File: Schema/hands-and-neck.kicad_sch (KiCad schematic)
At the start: 17 parts, among them U1 Left Arm Rotation X, U10 Right Arm Rotation Y, U11 Right Arm Rotation X, U12 Right Arm Rotation Z, U13 Right Elbow, U14 Neck Y, U15 Left Arm Rotation Y, U16 Neck Z, U2 Left Arm Rotation Z, U5 Left Elbow, U6 Left Wrist, U7 Left Claw, U8 Right Wrist, U9 Right Claw

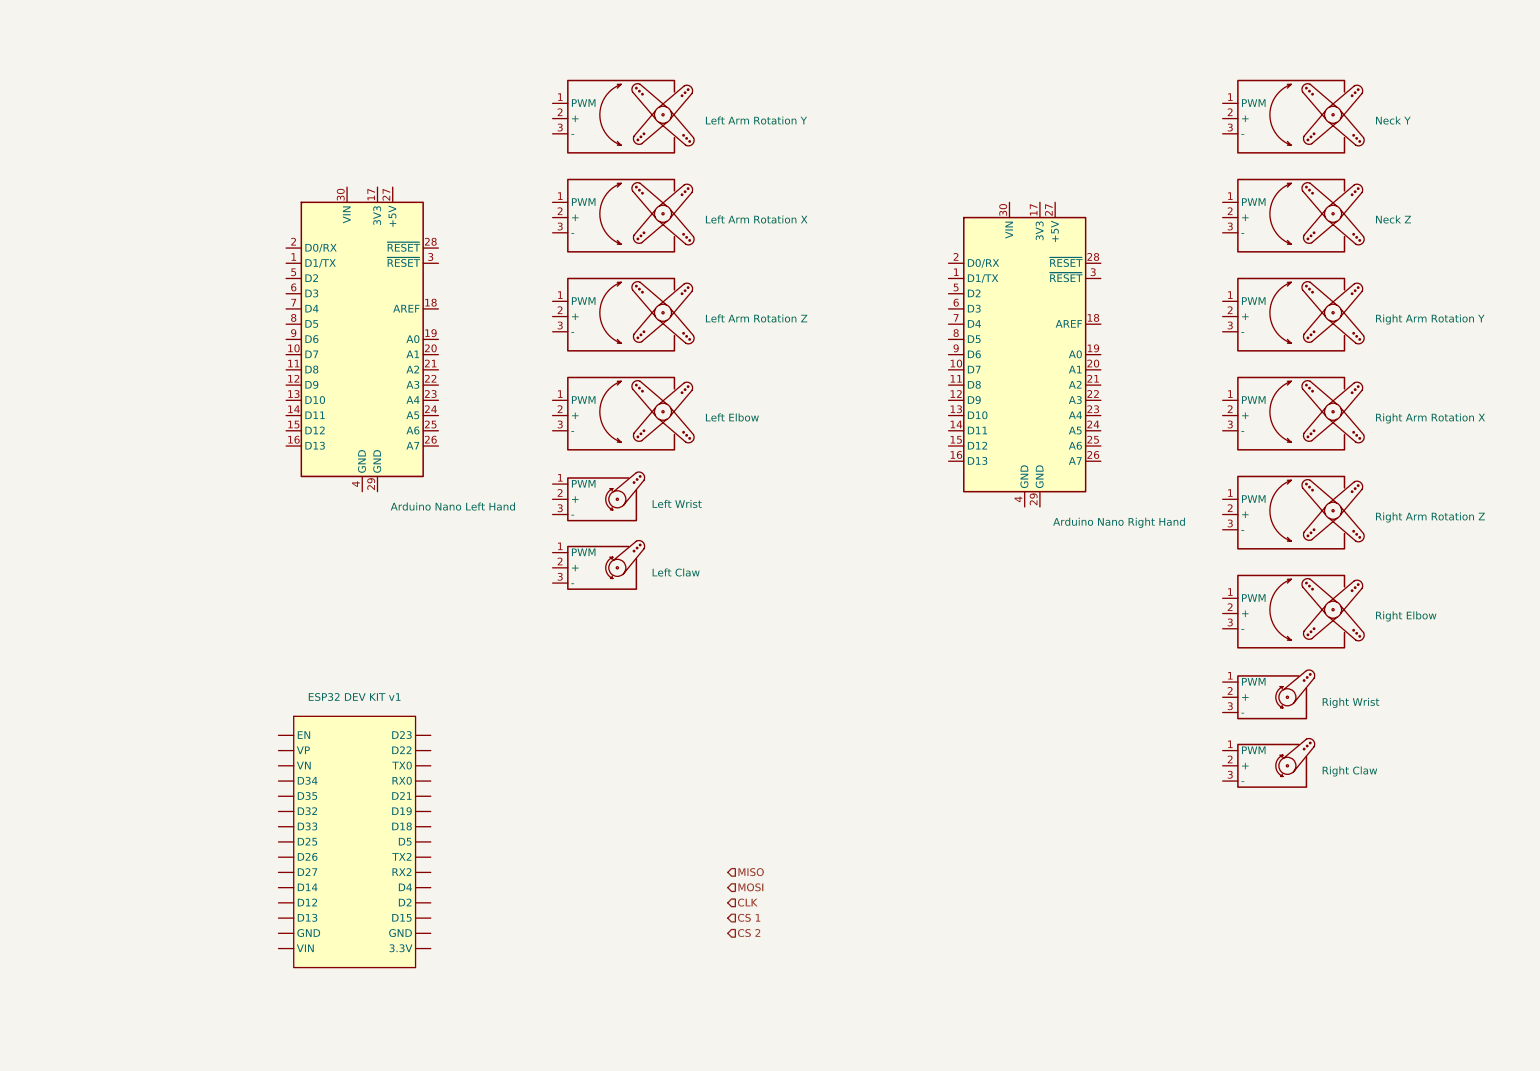
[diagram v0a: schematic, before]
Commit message: Updated schema and added math before ONCS
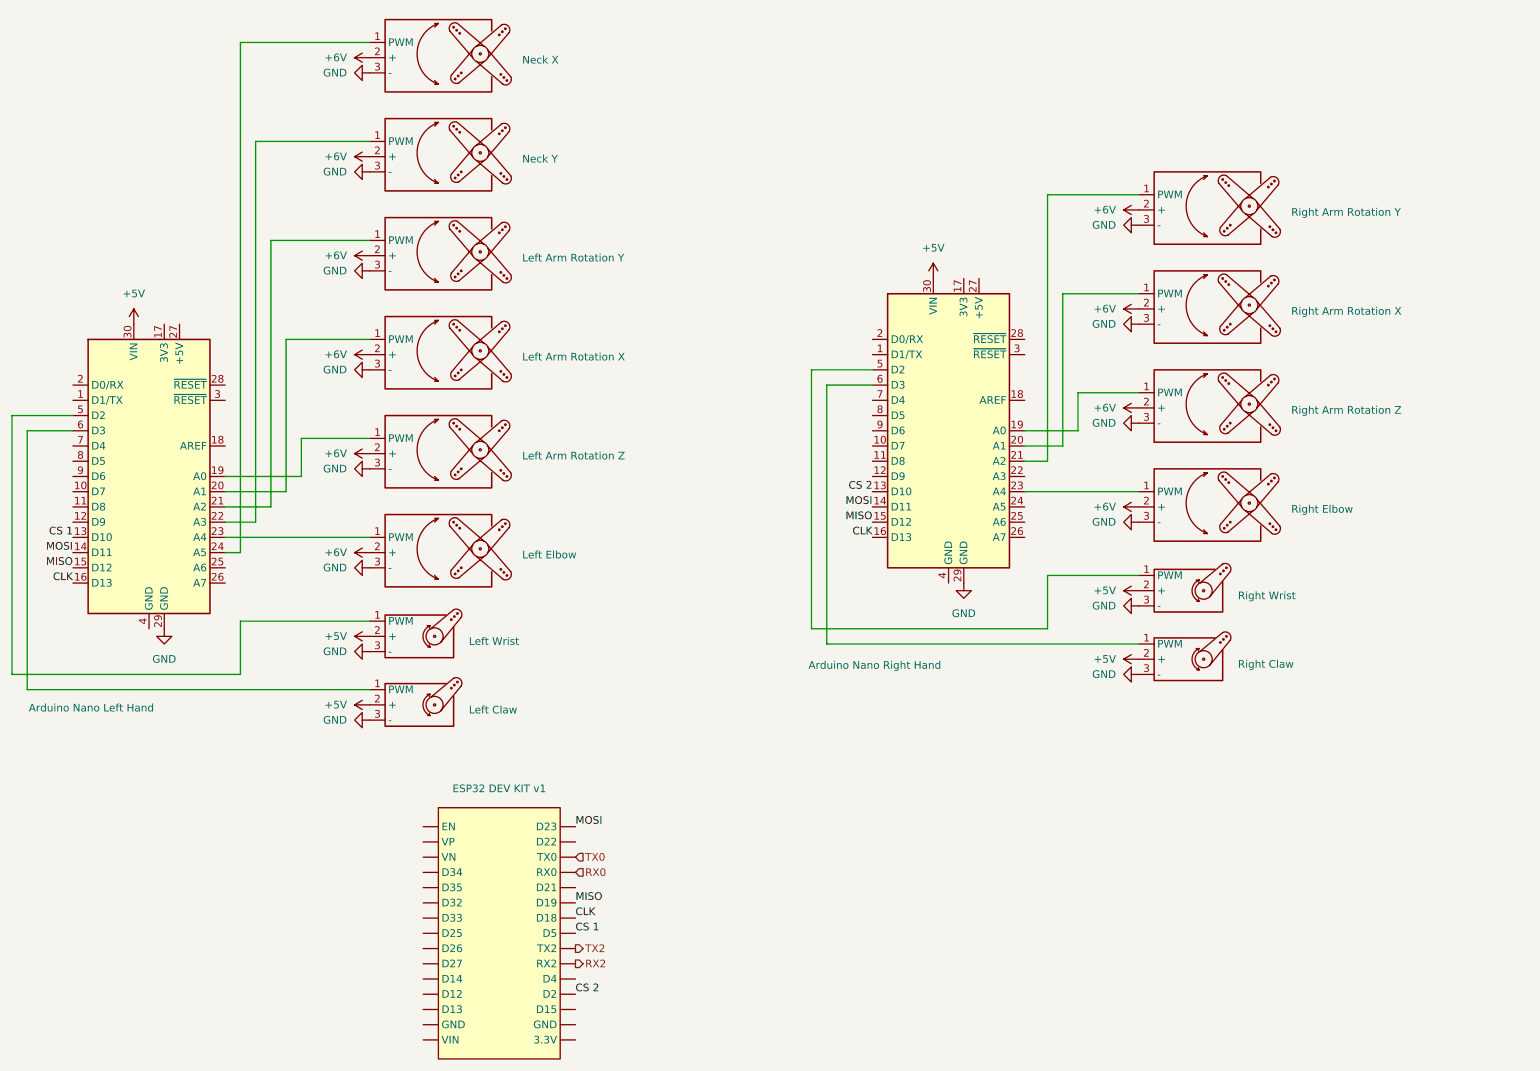
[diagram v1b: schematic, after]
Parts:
- removed A6: Arduino Nano Right Hand, Module:Arduino_Nano, symbol MCU_Module:Arduino_Nano_v3.x
- removed U10: Right Arm Rotation Y, symbol MARCEL-custom:Servo_Motor_MG996R
- removed U11: Right Arm Rotation X, symbol MARCEL-custom:Servo_Motor_MG996R
- added A3: Arduino Nano Right Hand, Module:Arduino_Nano, symbol MCU_Module:Arduino_Nano_v3.x
- added U18: Right Arm Rotation Z, symbol MARCEL-custom:Servo_Motor_MG996R
- added U19: Right Elbow, symbol MARCEL-custom:Servo_Motor_MG996R
- U12: value Right Arm Rotation Z -> Right Arm Rotation Y
- U13: value Right Elbow -> Right Arm Rotation X
- U14: value Neck Y -> Neck X
- U16: value Neck Z -> Neck Y
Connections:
- net CLK: now also A2.16 (D13), ESP32 DEV KIT v1. (VP), A3.16 (D13)
- net CS 1: now also A2.13 (D10), ESP32 DEV KIT v1. (VP)
- net CS 2: now also ESP32 DEV KIT v1. (VP), A3.13 (D10)
- net MISO: now also A2.15 (D12), ESP32 DEV KIT v1. (VP), A3.15 (D12)
- net MOSI: now also A2.14 (D11), ESP32 DEV KIT v1. (VP), A3.14 (D11)
- net at U2.1 (PWM): now also A2.19 (A0)
- net +6V: now reaches U2.2 (+)
- net +6V: now also U1.2 (+), U12.2 (+), U13.2 (+), U14.2 (+), U15.2 (+), U16.2 (+), U5.2 (+), U18.2 (+), U19.2 (+)
- net GND: now reaches U2.3 (-)
- net GND: now also A2.29 (GND), U1.3 (-), U12.3 (-), U13.3 (-), U14.3 (-), U15.3 (-), U16.3 (-), U5.3 (-), U6.3 (-), U7.3 (-), U8.3 (-), U9.3 (-), A3.29 (GND), U18.3 (-), U19.3 (-)
- net at U5.1 (PWM): now also A2.23 (A4)
- net at U6.1 (PWM): now also A2.5 (D2)
- net +5V: now reaches U6.2 (+)
- net +5V: now also A2.30 (VIN), U7.2 (+), U8.2 (+), U9.2 (+), A3.30 (VIN)
- net at U13.1 (PWM): now also A3.20 (A1)
- net TX2: now reaches ESP32 DEV KIT v1. (VP)
- net at U16.1 (PWM): now also A2.22 (A3)
- net at U14.1 (PWM): now also A2.24 (A5)
- net at U15.1 (PWM): now also A2.21 (A2)
- net at A2.20 (A1): now also U1.1 (PWM)
- net at A2.6 (D3): now also U7.1 (PWM)
- net at U12.1 (PWM): now also A3.21 (A2)
- net at U8.1 (PWM): now also A3.5 (D2)
- net at U9.1 (PWM): now also A3.6 (D3)
- new net: A3.19 (A0), U18.1 (PWM)
- new net: A3.23 (A4), U19.1 (PWM)
- new net RX0: ESP32 DEV KIT v1. (VP)
- new net RX2: ESP32 DEV KIT v1. (VP)
- new net TX0: ESP32 DEV KIT v1. (VP)
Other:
- moved on the sheet: ESP32 DEV KIT v1

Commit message: Robochallenge state
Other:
- title: (none) -> Hands and Neck
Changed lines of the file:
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@@
 	(generator_version "8.0")
 	(paper "A4")
+	(title_block
+		(title "Hands and Neck")
+		(date "08.05.2024")
+		(rev "1")
+		(comment 1 "The interaction schema")
+		(comment 2 "Controlls the hands and the head rotation")
+	)
 	(wire
 		(pts
